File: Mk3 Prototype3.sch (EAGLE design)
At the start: 149 parts, among them IC1 TPD3E001DRL, IC2 TPS62082, IC3 STM32F401V, IC4 BQ24092, IC6 CC3100MOD, IC7 BQ2970, IC8 LSM6DS3, IC9 LIS3MDL, J1 ZX62-AB-5PA(11), J2 ER-CON50HT-1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

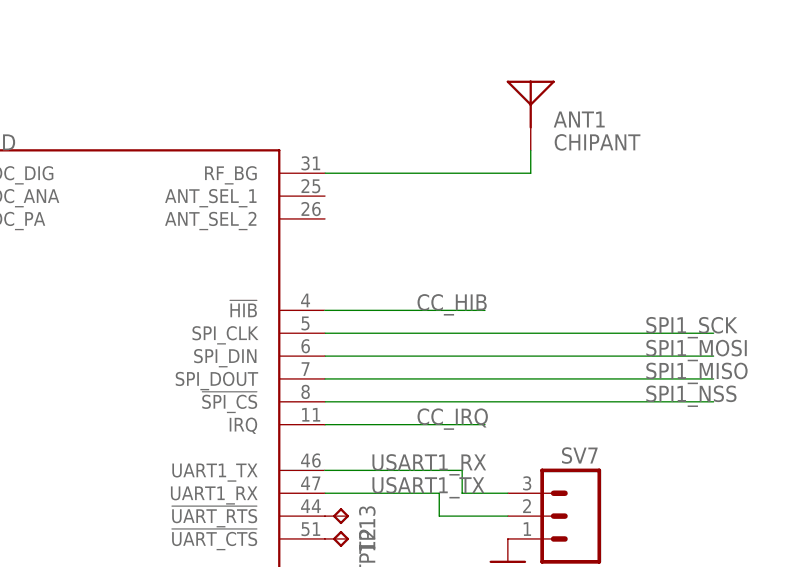
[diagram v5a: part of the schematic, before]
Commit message: added testpoint for !HIB
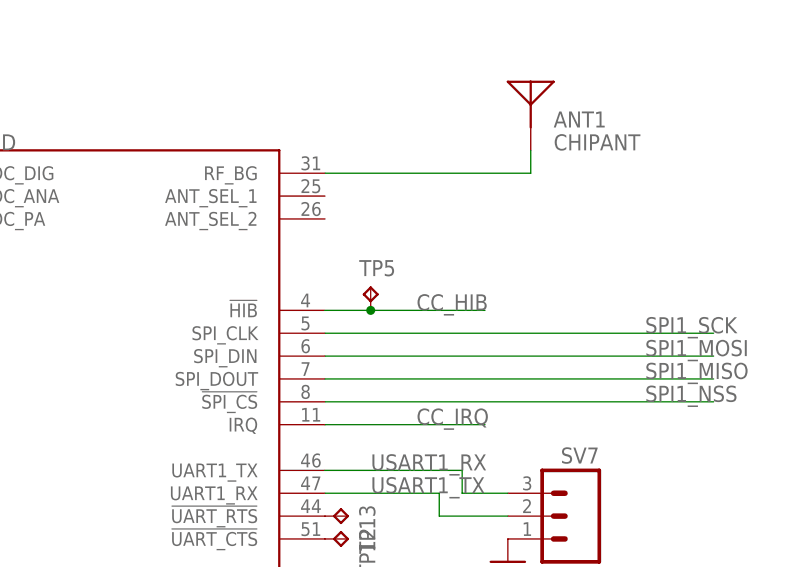
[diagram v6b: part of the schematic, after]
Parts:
- added TP5: TPB1,27, TiLDA Mk3 Parts:TPB1,27
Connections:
- net CC_HIB: now also TP5.TP
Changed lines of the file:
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@@
 <part name="D2" library="Diodes" deviceset="1N4148" device="-SOD123" value="NTS245SFT1G"/>
 <part name="TP4" library="TiLDA Mk3 Parts" deviceset="TP" device="B1,27"/>
+<part name="TP5" library="TiLDA Mk3 Parts" deviceset="TP" device="B1,27"/>
 </parts>
 <sheets>
@@
 <attribute name="NAME" x="732.79" y="135.89" size="1.778" layer="95" rot="R180"/>
 </instance>
+<instance part="TP5" gate="G$1" x="495.3" y="218.44" smashed="yes">
+<attribute name="NAME" x="494.03" y="219.71" size="1.778" layer="95"/>
+</instance>
 </instances>
 <busses>
@@
 <segment>
 <pinref part="IC6" gate="G$1" pin="!HIB"/>
-<wire x1="490.22" y1="215.9" x2="508" y2="215.9" width="0.1524" layer="91"/>
+<wire x1="490.22" y1="215.9" x2="495.3" y2="215.9" width="0.1524" layer="91"/>
 <label x="500.38" y="215.9" size="1.778" layer="95"/>
-</segment>
-<segment>
+<pinref part="TP5" gate="G$1" pin="TP"/>
+<wire x1="495.3" y1="215.9" x2="508" y2="215.9" width="0.1524" layer="91"/>
+<junction x="495.3" y="215.9"/>
+</segment>
+<segment>
